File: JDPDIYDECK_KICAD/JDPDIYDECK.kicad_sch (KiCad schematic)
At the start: 17 parts, among them J1 Conn_01x05, J2 Conn_01x05, J3 Conn_01x02, U1 NSL-32, U2 NSL-32, U3 TLV2372

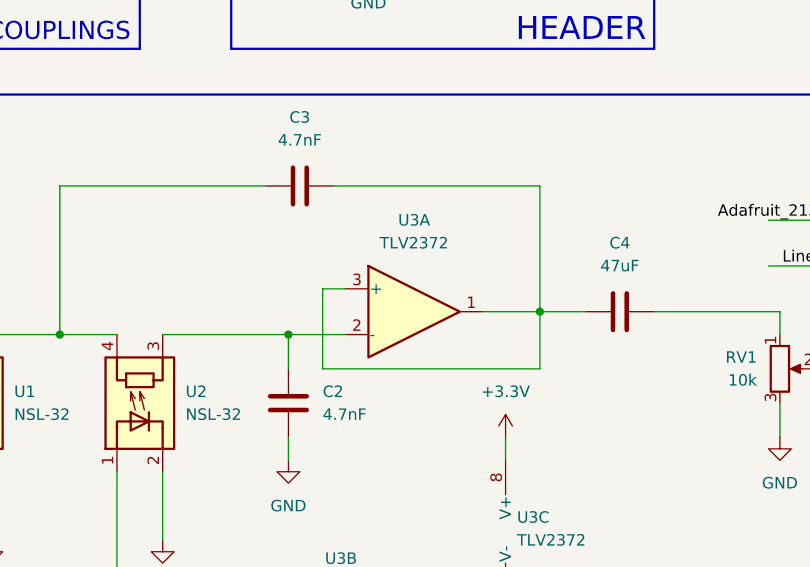
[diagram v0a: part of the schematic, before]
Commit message: amendments to op amp routing
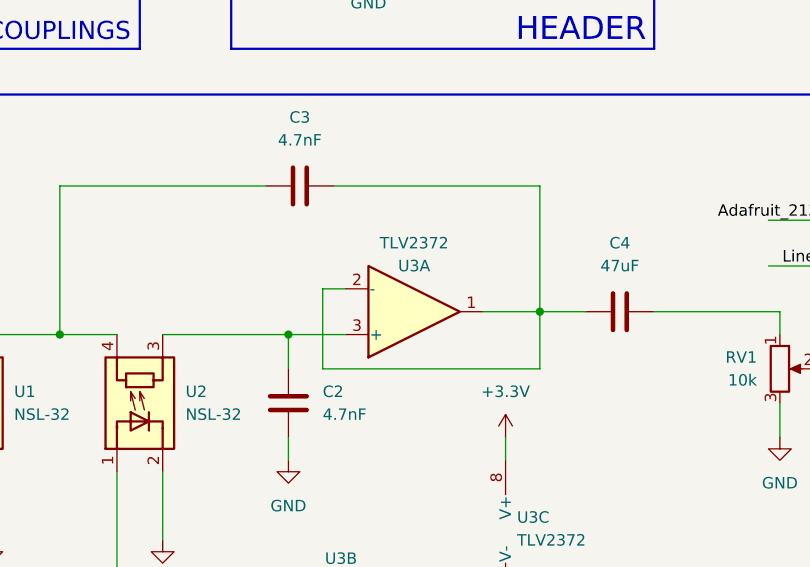
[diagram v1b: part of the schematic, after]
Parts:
- added unit 2 of U3
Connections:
- net OP2+: now also U3.5 (+); no longer U3.5 (+)
- net OP2-: now also U3.6 (-); no longer U3.6 (-)
- net OP2OUT: now also U3.7; no longer U3.7
- net at C2.1, U2.3 (R): now also U3.3 (+); no longer U3.2 (-)
- net at C3.1, C4.1, U3.1: now also U3.2 (-); no longer U3.3 (+)
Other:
- company: ECE304 JDP26 -> Vaikunth Elango
- title: ECE304_HW05 -> DIYDECK
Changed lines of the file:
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@@
 	(paper "A4")
 	(title_block
-		(title "ECE304_HW05")
-		(date "2026-03-03")
-		(rev "rev1")
-		(company "ECE304 JDP26")
-		(comment 1 "Osayogie Oyemwense")
-		(comment 2 "Vaikunth Elango")
+		(title "DIYDECK")
+		(date "2026-05-16")
+		(rev "rev2")
+		(company "Vaikunth Elango")
 	)
 	(rectangle
@@
 		(lib_id "Amplifier_Operational:TLV2372")
 		(at 167.64 111.76 0)
-		(unit 1)
-		(exclude_from_sim no)
-		(in_bom yes)
-		(on_board yes)
-		(dnp no)
-		(fields_autoplaced yes)
+		(mirror x)
+		(unit 1)
+		(exclude_from_sim no)
+		(in_bom yes)
+		(on_board yes)
+		(dnp no)
 		(property "Reference" "U3"
-			(at 167.64 101.6 0)
-			(effects
-				(font
+			(at 167.64 106.68 0)
+			(effects
+				(font
